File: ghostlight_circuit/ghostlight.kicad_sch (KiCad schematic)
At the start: 4 parts, among them IC2 MCP1700T-3302E_TT

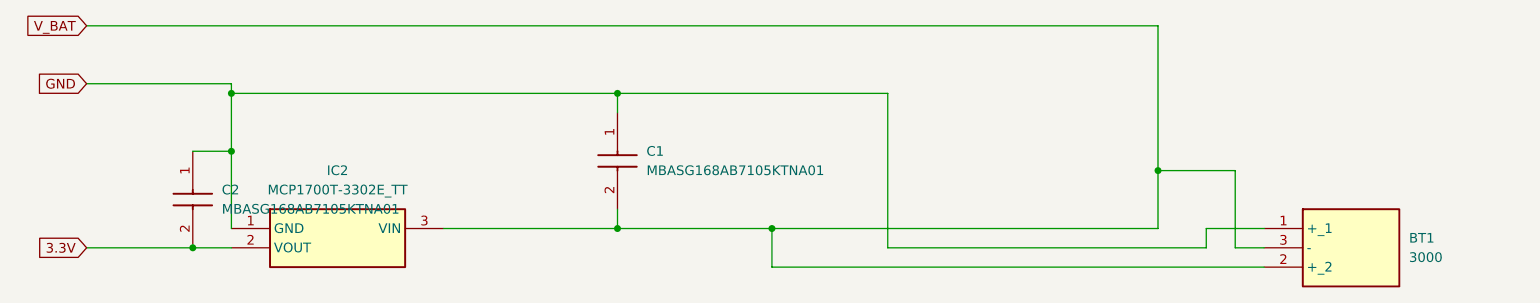
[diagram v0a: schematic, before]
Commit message: update pcb
rerout and connect accelerometer

better re-route
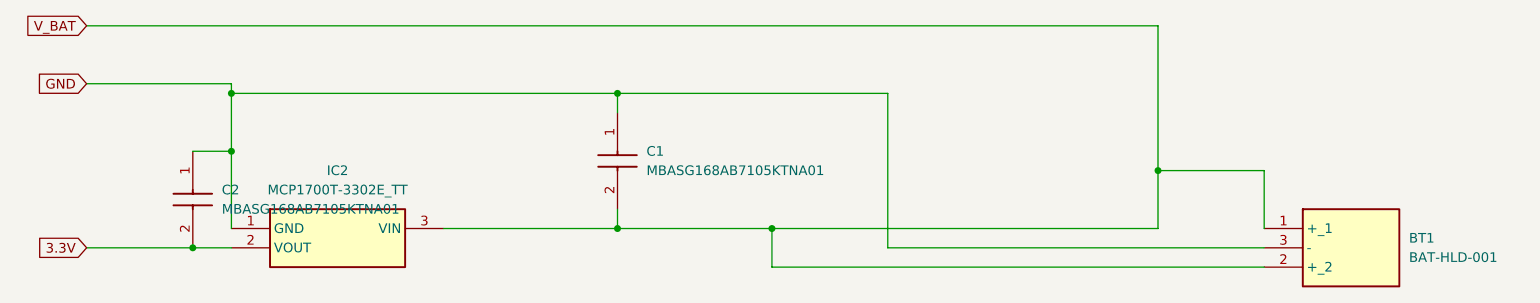
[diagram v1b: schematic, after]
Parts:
- removed BT1: 3000, custom_ring:Battery_Holder_Lynx_CR2032, symbol SamacSys_Parts:3000
- added BT1: BAT-HLD-001, custom_ring:BATHLD001mod, symbol SamacSys_Parts:BAT-HLD-001
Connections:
- net GND: now also BT1.3 (-)
- net V_BAT: now also BT1.1 (+_1), BT1.2 (+_2)
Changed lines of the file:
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@@
-	(wire
-		(pts
-			(xy 214.63 121.92) (xy 214.63 119.38)
-		)
-		(stroke
-			(width 0)
-			(type default)
-		)
-	)
-	(wire
-		(pts
-			(xy 222.25 121.92) (xy 218.44 121.92)
-		)
-		(stroke
-			(width 0)
-			(type default)
-		)
-	)
 	(wire
 		(pts
@@
 	(wire
 		(pts
-			(xy 218.44 111.76) (xy 208.28 111.76)
+			(xy 208.28 111.76) (xy 222.25 111.76)
 		)
 		(stroke
@@
 	(wire
 		(pts
-			(xy 214.63 119.38) (xy 222.25 119.38)
-		)
-		(stroke
-			(width 0)
-			(type default)
-		)
-	)
-	(wire
-		(pts
-			(xy 172.72 121.92) (xy 214.63 121.92)
-		)
-		(stroke
-			(width 0)
-			(type default)
-		)
-	)
-	(wire
-		(pts
-			(xy 218.44 121.92) (xy 218.44 111.76)
+			(xy 172.72 121.92) (xy 222.25 121.92)
 		)
 		(stroke
@@
 		(pts
 			(xy 137.16 116.84) (xy 137.16 119.38)
+		)
+		(stroke
+			(width 0)
+			(type default)
+		)
+	)
+	(wire
+		(pts
+			(xy 222.25 111.76) (xy 222.25 119.38)
 		)
 		(stroke
@@
 	)
 	(symbol
+		(lib_id "SamacSys_Parts:BAT-HLD-001")
+		(at 222.25 119.38 0)
+		(unit 1)
+		(body_style 1)
+		(exclude_from_sim no)
+		(in_bom yes)
+		(on_board yes)
+		(in_pos_files yes)
+		(dnp no)
+		(fields_autoplaced yes)
+		(property "Reference" "BT1"
+			(at 241.3 120.6499 0)
+			(show_name no)
+			(do_not_autoplace no)
+			(effects
+				(font
+					(size 1.27 1.27)
+				)
+				(justify left)
+			)
+		)
+		(property "Value" "BAT-HLD-001"
+			(at 241.3 123.1899 0)
+			(show_name no)
+			(do_not_autoplace no)
+			(effects
+				(font
+					(size 1.27 1.27)
+				)
+				(justify left)
+			)
+		)
+		(property "Footprint" "custom_ring:BATHLD001mod"
+			(at 241.3 214.3 0)
+			(hide yes)
+			(show_name no)
+			(do_not_autoplace no)
+			(effects
+				(font
+					(size 1.27 1.27)
+				)
+				(justify left top)
+			)
+		)
+		(property "Datasheet" "https://www.te.com/commerce/DocumentDelivery/DDEController?Action=showdoc&DocId=Customer+Drawing%7FC-BAT-HLD-001-xx%7FE%7Fpdf%7FEnglish%7FENG_CD_C-BAT-HLD-001-xx_E.pdf%7FBAT-HLD-001"
+			(at 241.3 314.3 0)
+			(hide yes)
+			(show_name no)
+			(do_not_autoplace no)
+			(effects
+				(font
+					(size 1.27 1.27)
+				)
+				(justify left top)
+			)
+		)
+		(property "Description" "Battery Holders, CR2032, 1 Position, Horizontal, Nickel, PCB Mount Alignment, Power, -40  257 F [-40  125 C]"
+			(at 222.25 119.38 0)
+			(hide yes)
+			(show_name no)
+			(do_not_autoplace no)
+			(effects
+				(font
+					(size 1.27 1.27)
+				)
+			)
+		)
+		(property "Height" "4.3"
+			(at 241.3 514.3 0)
+			(hide yes)
+			(show_name no)
+			(do_not_autoplace no)
+			(effects
+				(font
+					(size 1.27 1.27)
+				)
+				(justify left top)
+			)
+		)
+		(property "Mouser Part Number" "712-BAT-HLD-001"
+			(at 241.3 614.3 0)
+			(hide yes)
+			(show_name no)
+			(do_not_autoplace no)
+			(effects
+				(font
+					(size 1.27 1.27)
+				)
+				(justify left top)
+			)
+		)
+		(property "Mouser Price/Stock" "https://www.mouser.co.uk/ProductDetail/TE-Connectivity-Linx-Technologies/BAT-HLD-001?qs=K5ta8V%252BWhta7hbVGfm4dqA%3D%3D"
+			(at 241.3 714.3 0)
+			(hide yes)
+			(show_name no)
+			(do_not_autoplace no)
+			(effects
+				(font
+					(size 1.27 1.27)
+				)
+				(justify left top)
+			)
+		)
+		(property "Manufacturer_Name" "TE Connectivity"
+			(at 241.3 814.3 0)
+			(hide yes)
+			(show_name no)
+			(do_not_autoplace no)
+			(effects
+				(font
+					(size 1.27 1.27)
+				)
+				(justify left top)
+			)
+		)
+		(property "Manufacturer_Part_Number" "BAT-HLD-001"
+			(at 241.3 914.3 0)
+			(hide yes)
+			(show_name no)
+			(do_not_autoplace no)
+			(effects
+				(font
+					(size 1.27 1.27)
+				)
+				(justify left top)
+			)
+		)
+		(pin "1"
+		)
+		(pin "3"
+		)
+		(pin "2"
+		)
+		(instances
+			(project "ghostlight"
+				(path "/c84668a1-6299-4dd7-b9cf-055166213e49"
+					(reference "BT1")
+					(unit 1)
+				)
+			)
+		)
+	)
+	(symbol
 		(lib_id "SamacSys_Parts:MBASG168AB7105KTNA01")
 		(at 137.16 104.14 270)
@@
 					(unit 1)
 				)
-			)
-		)
-	)
-	(symbol
-		(lib_id "SamacSys_Parts:3000")
-		(at 222.25 119.38 0)
-		(unit 1)
-		(body_style 1)
-		(exclude_from_sim no)
-		(in_bom yes)
-		(on_board yes)
-		(in_pos_files yes)
-		(dnp no)
-		(fields_autoplaced yes)
-		(property "Reference" "BT1"
-			(at 241.3 120.6499 0)
-			(show_name no)
-			(do_not_autoplace no)
-			(effects
-				(font
-					(size 1.27 1.27)
-				)
-				(justify left)
-			)
-		)
-		(property "Value" "3000"
-			(at 241.3 123.1899 0)
-			(show_name no)
-			(do_not_autoplace no)
-			(effects
-				(font
-					(size 1.27 1.27)
-				)
-				(justify left)
-			)
-		)
-		(property "Footprint" "custom_ring:Battery_Holder_Lynx_CR2032"
-			(at 241.3 214.3 0)
-			(hide yes)
-			(show_name no)
-			(do_not_autoplace no)
-			(effects
-				(font
-					(size 1.27 1.27)
-				)
-				(justify left top)
-			)
-		)
-		(property "Datasheet" "https://www.keyelco.com/product-pdf.cfm?p=777"
-			(at 241.3 314.3 0)
-			(hide yes)
-			(show_name no)
-			(do_not_autoplace no)
-			(effects
-				(font
-					(size 1.27 1.27)
-				)
-				(justify left top)
-			)
-		)
-		(property "Description" "KEYSTONE - 3000 - Battery Contact, Coin Cell - 12mm, SMD, Phosphor Bronze"
-			(at 222.25 119.38 0)
-			(hide yes)
-			(show_name no)
-			(do_not_autoplace no)
-			(effects
-				(font
-					(size 1.27 1.27)
-				)
-			)
-		)
-		(property "Height" "3.43"
-			(at 241.3 514.3 0)
-			(hide yes)
-			(show_name no)
-			(do_not_autoplace no)
-			(effects
-				(font
-					(size 1.27 1.27)
-				)
-				(justify left top)
-			)
-		)
-		(property "Mouser Part Number" "534-3000"
-			(at 241.3 614.3 0)
-			(hide yes)
-			(show_name no)
-			(do_not_autoplace no)
-			(effects
-				(font
-					(size 1.27 1.27)
-				)
-				(justify left top)
-			)
-		)
-		(property "Mouser Price/Stock" "https://www.mouser.co.uk/ProductDetail/Keystone-Electronics/3000?qs=Mn60vILZNNbcLh3ZnzbtUw%3D%3D"
-			(at 241.3 714.3 0)
-			(hide yes)
-			(show_name no)
-			(do_not_autoplace no)
-			(effects
-				(font
-					(size 1.27 1.27)
-				)
-				(justify left top)
-			)
-		)
-		(property "Manufacturer_Name" "Keystone Electronics"
-			(at 241.3 814.3 0)
-			(hide yes)
-			(show_name no)
-			(do_not_autoplace no)
-			(effects
-				(font
-					(size 1.27 1.27)
-				)
-				(justify left top)
-			)
-		)
-		(property "Manufacturer_Part_Number" "3000"
-			(at 241.3 914.3 0)
-			(hide yes)
-			(show_name no)
-			(do_not_autoplace no)
-			(effects
-				(font
-					(size 1.27 1.27)
-				)
-				(justify left top)
-			)
-		)
-		(pin "2"
-		)
-		(pin "1"
-		)
-		(pin "3"
-		)
-		(instances
-			(project "ghostlight"
-				(path "/c84668a1-6299-4dd7-b9cf-055166213e49"
-					(reference "BT1")
-					(unit 1)
-				)
